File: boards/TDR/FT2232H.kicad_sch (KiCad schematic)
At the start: 33 parts, among them U11 93LCxxBxxOT, U12 FT2232HL, U13 MIC5504-3.3YM5, Y1 12MHz

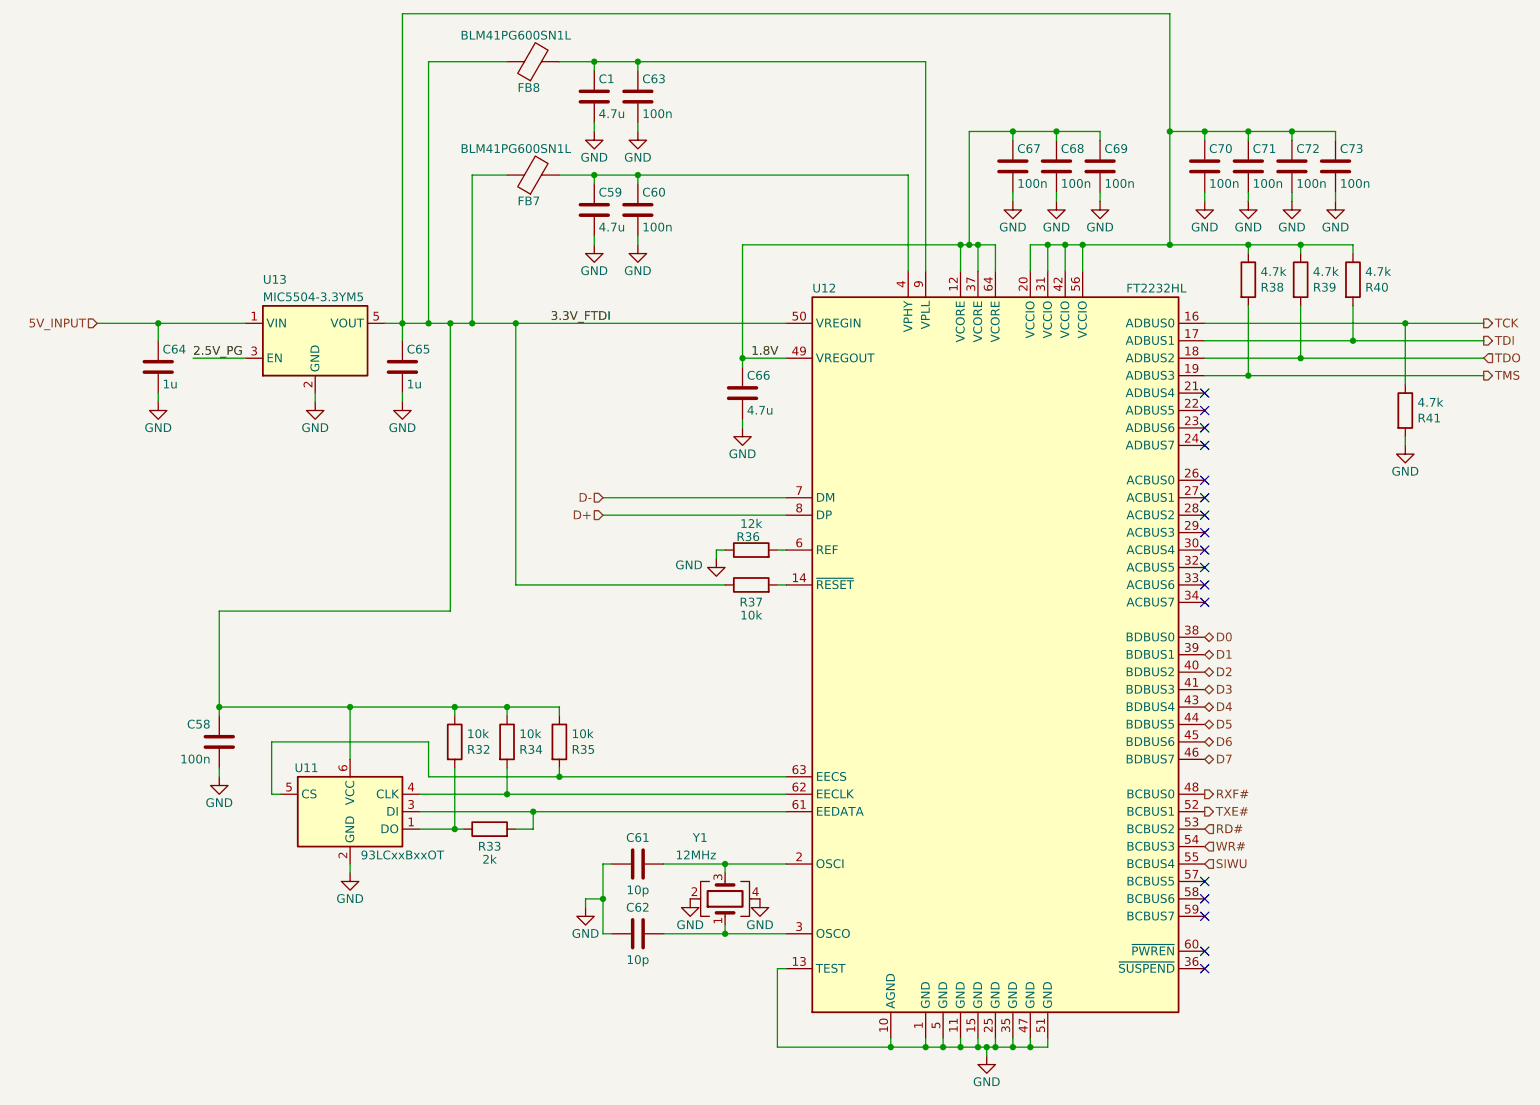
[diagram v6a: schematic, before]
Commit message: Add LD39050PUR feedback resistor values, fixed regulator enable
Fixes #1
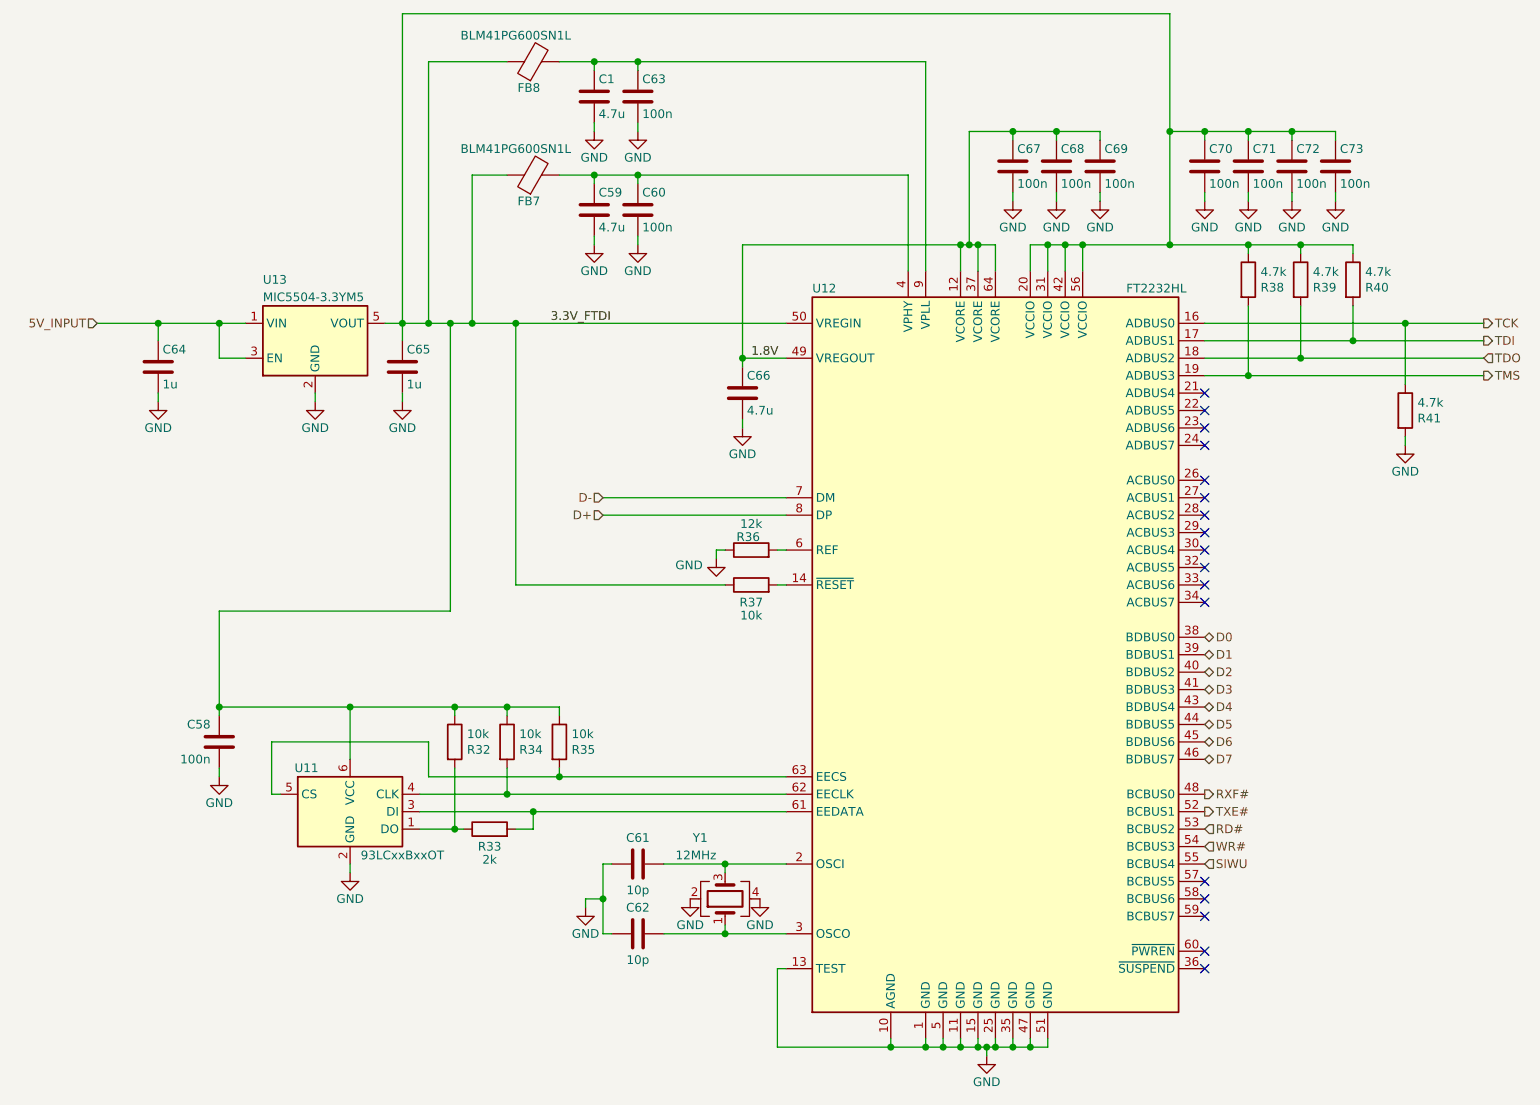
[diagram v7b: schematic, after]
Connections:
- net 2.5V_PG is gone; now on net 5V_INPUT: U13.3 (EN)
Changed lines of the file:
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@@
-(kicad_sch (version 20200618) (host eeschema "(5.99.0-2250-gafd432e68)")
+(kicad_sch (version 20200714) (host eeschema "(5.99.0-2491-g71882a7b0)")
   (page 2 5)
   (paper "A4")
@@
     (comment 4 "EN")
   )
-  (junction (at 46.99 58.42) (diameter 0) (color 0 0 0 0))
-  (junction (at 55.88 114.3) (diameter 0) (color 0 0 0 0))
-  (junction (at 74.93 114.3) (diameter 0) (color 0 0 0 0))
-  (junction (at 82.55 58.42) (diameter 0) (color 0 0 0 0))
-  (junction (at 86.36 58.42) (diameter 0) (color 0 0 0 0))
-  (junction (at 89.535 58.42) (diameter 0) (color 0 0 0 0))
-  (junction (at 90.17 114.3) (diameter 0) (color 0 0 0 0))
-  (junction (at 90.17 132.08) (diameter 0) (color 0 0 0 0))
-  (junction (at 92.71 58.42) (diameter 0) (color 0 0 0 0))
-  (junction (at 97.79 114.3) (diameter 0) (color 0 0 0 0))
-  (junction (at 97.79 127) (diameter 0) (color 0 0 0 0))
-  (junction (at 99.06 58.42) (diameter 0) (color 0 0 0 0))
-  (junction (at 101.6 129.54) (diameter 0) (color 0 0 0 0))
-  (junction (at 105.41 124.46) (diameter 0) (color 0 0 0 0))
-  (junction (at 110.49 20.32) (diameter 0) (color 0 0 0 0))
-  (junction (at 110.49 36.83) (diameter 0) (color 0 0 0 0))
-  (junction (at 111.76 142.24) (diameter 0) (color 0 0 0 0))
-  (junction (at 116.84 20.32) (diameter 0) (color 0 0 0 0))
-  (junction (at 116.84 36.83) (diameter 0) (color 0 0 0 0))
-  (junction (at 129.54 137.16) (diameter 0) (color 0 0 0 0))
-  (junction (at 129.54 147.32) (diameter 0) (color 0 0 0 0))
-  (junction (at 132.08 63.5) (diameter 0) (color 0 0 0 0))
-  (junction (at 153.67 163.83) (diameter 0) (color 0 0 0 0))
-  (junction (at 158.75 163.83) (diameter 0) (color 0 0 0 0))
-  (junction (at 161.29 163.83) (diameter 0) (color 0 0 0 0))
-  (junction (at 163.83 46.99) (diameter 0) (color 0 0 0 0))
-  (junction (at 163.83 163.83) (diameter 0) (color 0 0 0 0))
-  (junction (at 165.1 46.99) (diameter 0) (color 0 0 0 0))
-  (junction (at 166.37 46.99) (diameter 0) (color 0 0 0 0))
-  (junction (at 166.37 163.83) (diameter 0) (color 0 0 0 0))
-  (junction (at 167.64 163.83) (diameter 0) (color 0 0 0 0))
-  (junction (at 168.91 163.83) (diameter 0) (color 0 0 0 0))
-  (junction (at 171.45 30.48) (diameter 0) (color 0 0 0 0))
-  (junction (at 171.45 163.83) (diameter 0) (color 0 0 0 0))
-  (junction (at 173.99 163.83) (diameter 0) (color 0 0 0 0))
-  (junction (at 176.53 46.99) (diameter 0) (color 0 0 0 0))
-  (junction (at 177.8 30.48) (diameter 0) (color 0 0 0 0))
-  (junction (at 179.07 46.99) (diameter 0) (color 0 0 0 0))
-  (junction (at 181.61 46.99) (diameter 0) (color 0 0 0 0))
-  (junction (at 194.31 30.48) (diameter 0) (color 0 0 0 0))
-  (junction (at 194.31 46.99) (diameter 0) (color 0 0 0 0))
-  (junction (at 199.39 30.48) (diameter 0) (color 0 0 0 0))
-  (junction (at 205.74 30.48) (diameter 0) (color 0 0 0 0))
-  (junction (at 205.74 46.99) (diameter 0) (color 0 0 0 0))
-  (junction (at 205.74 66.04) (diameter 0) (color 0 0 0 0))
-  (junction (at 212.09 30.48) (diameter 0) (color 0 0 0 0))
-  (junction (at 213.36 46.99) (diameter 0) (color 0 0 0 0))
-  (junction (at 213.36 63.5) (diameter 0) (color 0 0 0 0))
-  (junction (at 220.98 60.96) (diameter 0) (color 0 0 0 0))
-  (junction (at 228.6 58.42) (diameter 0) (color 0 0 0 0))
-  (no_connect (at 199.39 142.24))
+  (junction (at 46.99 58.42) (diameter 1.016) (color 0 0 0 0))
+  (junction (at 55.88 58.42) (diameter 1.016) (color 0 0 0 0))
+  (junction (at 55.88 114.3) (diameter 1.016) (color 0 0 0 0))
+  (junction (at 74.93 114.3) (diameter 1.016) (color 0 0 0 0))
+  (junction (at 82.55 58.42) (diameter 1.016) (color 0 0 0 0))
+  (junction (at 86.36 58.42) (diameter 1.016) (color 0 0 0 0))
+  (junction (at 89.535 58.42) (diameter 1.016) (color 0 0 0 0))
+  (junction (at 90.17 114.3) (diameter 1.016) (color 0 0 0 0))
+  (junction (at 90.17 132.08) (diameter 1.016) (color 0 0 0 0))
+  (junction (at 92.71 58.42) (diameter 1.016) (color 0 0 0 0))
+  (junction (at 97.79 114.3) (diameter 1.016) (color 0 0 0 0))
+  (junction (at 97.79 127) (diameter 1.016) (color 0 0 0 0))
+  (junction (at 99.06 58.42) (diameter 1.016) (color 0 0 0 0))
+  (junction (at 101.6 129.54) (diameter 1.016) (color 0 0 0 0))
+  (junction (at 105.41 124.46) (diameter 1.016) (color 0 0 0 0))
+  (junction (at 110.49 20.32) (diameter 1.016) (color 0 0 0 0))
+  (junction (at 110.49 36.83) (diameter 1.016) (color 0 0 0 0))
+  (junction (at 111.76 142.24) (diameter 1.016) (color 0 0 0 0))
+  (junction (at 116.84 20.32) (diameter 1.016) (color 0 0 0 0))
+  (junction (at 116.84 36.83) (diameter 1.016) (color 0 0 0 0))
+  (junction (at 129.54 137.16) (diameter 1.016) (color 0 0 0 0))
+  (junction (at 129.54 147.32) (diameter 1.016) (color 0 0 0 0))
+  (junction (at 132.08 63.5) (diameter 1.016) (color 0 0 0 0))
+  (junction (at 153.67 163.83) (diameter 1.016) (color 0 0 0 0))
+  (junction (at 158.75 163.83) (diameter 1.016) (color 0 0 0 0))
+  (junction (at 161.29 163.83) (diameter 1.016) (color 0 0 0 0))
+  (junction (at 163.83 46.99) (diameter 1.016) (color 0 0 0 0))
+  (junction (at 163.83 163.83) (diameter 1.016) (color 0 0 0 0))
+  (junction (at 165.1 46.99) (diameter 1.016) (color 0 0 0 0))
+  (junction (at 166.37 46.99) (diameter 1.016) (color 0 0 0 0))
+  (junction (at 166.37 163.83) (diameter 1.016) (color 0 0 0 0))
+  (junction (at 167.64 163.83) (diameter 1.016) (color 0 0 0 0))
+  (junction (at 168.91 163.83) (diameter 1.016) (color 0 0 0 0))
+  (junction (at 171.45 30.48) (diameter 1.016) (color 0 0 0 0))
+  (junction (at 171.45 163.83) (diameter 1.016) (color 0 0 0 0))
+  (junction (at 173.99 163.83) (diameter 1.016) (color 0 0 0 0))
+  (junction (at 176.53 46.99) (diameter 1.016) (color 0 0 0 0))
+  (junction (at 177.8 30.48) (diameter 1.016) (color 0 0 0 0))
+  (junction (at 179.07 46.99) (diameter 1.016) (color 0 0 0 0))
+  (junction (at 181.61 46.99) (diameter 1.016) (color 0 0 0 0))
+  (junction (at 194.31 30.48) (diameter 1.016) (color 0 0 0 0))
+  (junction (at 194.31 46.99) (diameter 1.016) (color 0 0 0 0))
+  (junction (at 199.39 30.48) (diameter 1.016) (color 0 0 0 0))
+  (junction (at 205.74 30.48) (diameter 1.016) (color 0 0 0 0))
+  (junction (at 205.74 46.99) (diameter 1.016) (color 0 0 0 0))
+  (junction (at 205.74 66.04) (diameter 1.016) (color 0 0 0 0))
+  (junction (at 212.09 30.48) (diameter 1.016) (color 0 0 0 0))
+  (junction (at 213.36 46.99) (diameter 1.016) (color 0 0 0 0))
+  (junction (at 213.36 63.5) (diameter 1.016) (color 0 0 0 0))
+  (junction (at 220.98 60.96) (diameter 1.016) (color 0 0 0 0))
+  (junction (at 228.6 58.42) (diameter 1.016) (color 0 0 0 0))
+  (no_connect (at 199.39 83.82))
+  (no_connect (at 199.39 68.58))
+  (no_connect (at 199.39 93.98))
+  (no_connect (at 199.39 81.28))
+  (no_connect (at 199.39 149.86))
+  (no_connect (at 199.39 76.2))
   (no_connect (at 199.39 96.52))
-  (no_connect (at 199.39 91.44))
   (no_connect (at 199.39 88.9))
   (no_connect (at 199.39 71.12))
-  (no_connect (at 199.39 68.58))
-  (no_connect (at 199.39 93.98))
+  (no_connect (at 199.39 139.7))
   (no_connect (at 199.39 73.66))
-  (no_connect (at 199.39 83.82))
+  (no_connect (at 199.39 142.24))
+  (no_connect (at 199.39 91.44))
+  (no_connect (at 199.39 86.36))
   (no_connect (at 199.39 152.4))
   (no_connect (at 199.39 99.06))
-  (no_connect (at 199.39 149.86))
-  (no_connect (at 199.39 81.28))
-  (no_connect (at 199.39 76.2))
   (no_connect (at 199.39 144.78))
-  (no_connect (at 199.39 86.36))
-  (no_connect (at 199.39 139.7))
   (wire (pts (xy 38.1 58.42) (xy 46.99 58.42))
     (stroke (width 0) (type solid) (color 0 0 0 0))
   )
-  (wire (pts (xy 46.99 58.42) (xy 59.69 58.42))
+  (wire (pts (xy 46.99 58.42) (xy 55.88 58.42))
     (stroke (width 0) (type solid) (color 0 0 0 0))
   )
@@
     (stroke (width 0) (type solid) (color 0 0 0 0))
   )
-  (wire (pts (xy 52.07 63.5) (xy 59.69 63.5))
+  (wire (pts (xy 55.88 58.42) (xy 55.88 63.5))
+    (stroke (width 0) (type solid) (color 0 0 0 0))
+  )
+  (wire (pts (xy 55.88 58.42) (xy 59.69 58.42))
     (stroke (width 0) (type solid) (color 0 0 0 0))
   )
@@
     (stroke (width 0) (type solid) (color 0 0 0 0))
   )
+  (wire (pts (xy 59.69 63.5) (xy 55.88 63.5))
+    (stroke (width 0) (type solid) (color 0 0 0 0))
+  )
   (wire (pts (xy 63.5 119.38) (xy 86.36 119.38))
     (stroke (width 0) (type solid) (color 0 0 0 0))
@@
     (stroke (width 0) (type solid) (color 0 0 0 0))
   )
-  (label "2.5V_PG" (at 52.07 63.5 0)
-    (effects (font (size 1.27 1.27)) (justify left bottom))
-  )
   (label "3.3V_FTDI" (at 104.14 58.42 0)
